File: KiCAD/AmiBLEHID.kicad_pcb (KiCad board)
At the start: 2 copper layers, 31 x 35 mm, 10 parts, among them J1 D-Sub Female, SW1 Reset, SW2 Mode, U1 ESP32-H2-Zero, U2 74HC05

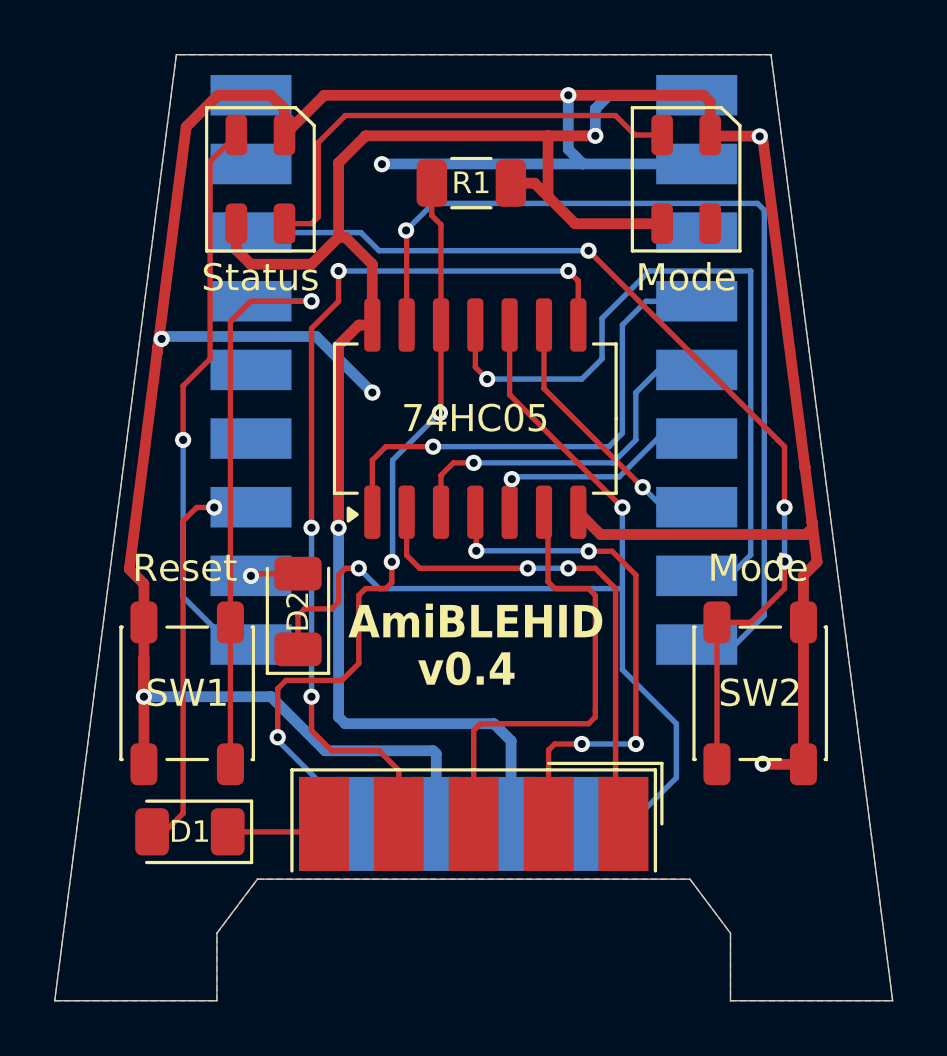
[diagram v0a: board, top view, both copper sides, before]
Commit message: v0.5 PCB layout, more compact design to fit A600
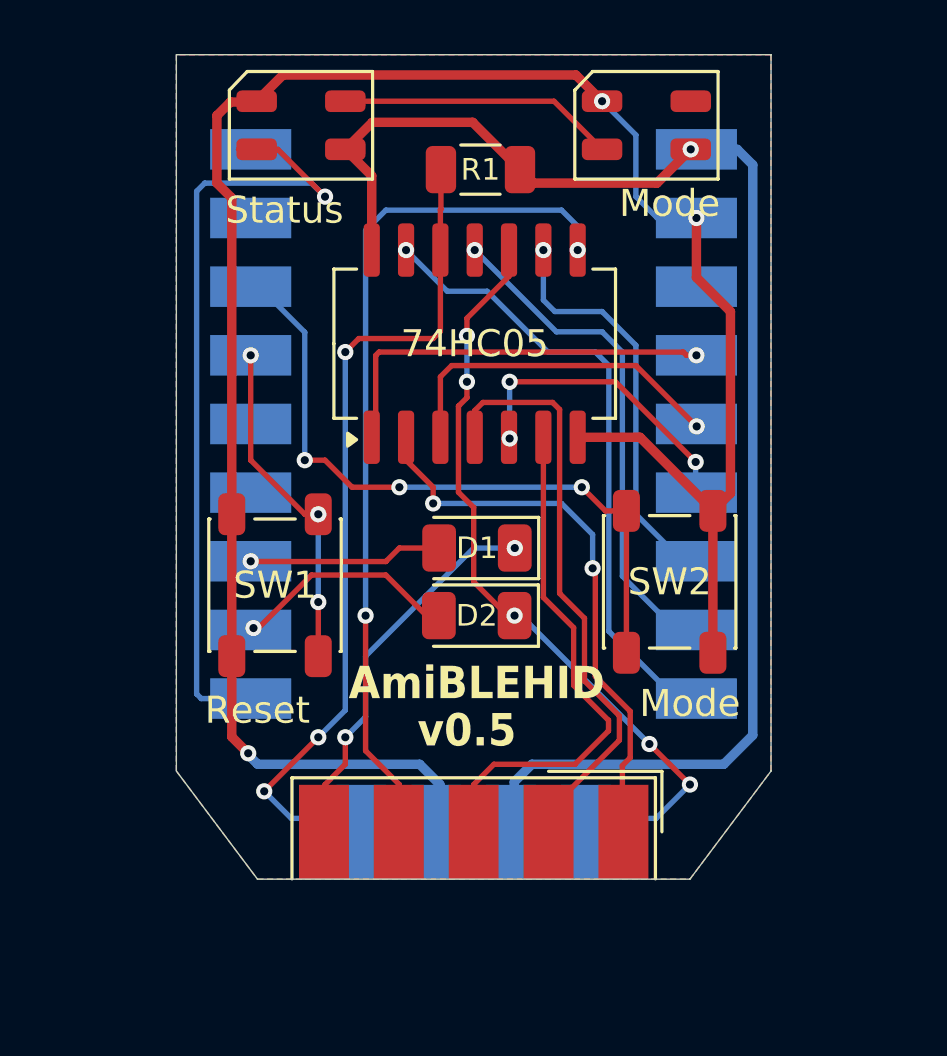
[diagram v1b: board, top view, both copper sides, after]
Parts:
- moved D1 14.9 mm to (95.1, 55.8)
- moved D2 6.61 mm to (95.1, 58.2), turned to 180 degrees
- moved SW2 5.31 mm to (102.2, 57.0)
- moved SW1 5.15 mm to (87.7, 57.1)
- moved U2 2.77 mm to (95.0, 48.2)
- moved LED1 2.50 mm to (88.6, 40.1), turned to 180 degrees
- moved LED2 2.48 mm to (101.4, 40.1), turned to 180 degrees
- moved U1 2.00 mm to (95.5, 50.9)
- moved R1 0.60 mm to (95.2, 41.8)
- moved J1 0.29 mm to (95.0, 66.2)
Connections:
- D1 pad 1: J_POTY -> J_POTX
- J1 pad 5: J_POTY -> J_POTX
- J1 pad 9: J_POTX -> J_POTY
- R1 pad 2: J_POTX -> J_POTY
- U2 pad 12: J_POTX -> J_POTY
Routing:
- net GND: track 122.9 -> 78.6 mm, vias 7 -> 3
- net J_POTY: track 4.14 -> 31.7 mm, vias 0 -> 3
- net J_LEFT: track 3.16 -> 19.7 mm
- net J_POTX: track 29.3 -> 14.3 mm, vias 3 -> 2
- net Net-(U1-IO5): track 35.2 -> 23.4 mm
- net Net-(SW2-A): track 36.5 -> 25.4 mm
- net Net-(SW1-A): track 22.7 -> 12.5 mm, vias 1 -> 3
- net Net-(LED1-DIN): track 21.1 -> 29.7 mm
- net J_FIRE: track 37.5 -> 29.1 mm, vias 2 -> 5
- net Net-(U1-IO4): track 27.3 -> 18.9 mm
- net J_UP: track 12.7 -> 20.9 mm
- net Net-(LED1-DOUT): track 17.5 -> 10.2 mm
- net Net-(D2-A): track 1.77 -> 8.42 mm
- net +5V: track 60.5 -> 54.8 mm, vias 2 -> 1
- net Net-(D1-A): track 13.1 -> 7.86 mm
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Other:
- board size 31 x 35 mm -> 22 x 30.5 mm
- board text added: "v0.5"
- board text removed: "v0.4"
